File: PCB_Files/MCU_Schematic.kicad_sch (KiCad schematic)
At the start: 34 parts, among them J10 Conn_01x04_Pin, J2 Conn_01x04_Socket, J3 Conn_01x08_Socket, J5 USB_C_Receptacle_USB2.0_16P, J6 Conn_01x04_Socket, J9 Conn_01x04_Socket, SW1 SW_SPDT, U2 STM32F411RETx, Y1 16MHz

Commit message: Swapped all +3.3V and +3.3VA labels to +3V3 and +3V3A lables for clarity.
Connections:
- net +3.3V renamed +3V3
- net +3.3VA renamed +3V3A
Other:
- note added: "+3V31"
- note removed: "+3.31v"

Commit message: Changed pin names on MCU sheet for clarity. Example: US_TIM3_CH1 to US_ECHO
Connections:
- net USB_VSENSE: now reaches R10.1, R9.1, U2.43 (PA10)
- net USB_VBUS: now reaches J5.A4 (VBUS), J5.A9 (VBUS), J5.B4 (VBUS), J5.B9 (VBUS), R9.2
- net TIM2_CH2: now reaches U2.15 (PA1)
- net ECHO_5V: now reaches J2.2 (Pin_2), R3.2
- net US_TIM3_CH1 renamed US_ECHO
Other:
- note removed: "+3V31"
- note removed: "+5V"
- note removed: "+5V Echo"
- note removed: "Use voltage divider for VBUS to GPIO"
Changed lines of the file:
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@@
-		)
-	)
-	(text "Use voltage divider for VBUS to GPIO"
-		(exclude_from_sim no)
-		(at 208.915 67.945 0)
-		(effects
-			(font
-				(size 1.27 1.27)
-			)
 		)
 	)
@@
 		)
 	)
-	(text "+3V31"
-		(exclude_from_sim no)
-		(at 234.315 62.23 0)
-		(effects
-			(font
-				(size 1.016 1.016)
-				(thickness 0.1429)
-			)
-		)
-	)
 	(text "Ultrasonic Sensor"
 		(exclude_from_sim no)
@@
 		)
 	)
-	(text "+5V Echo"
-		(exclude_from_sim no)
-		(at 250.19 36.195 0)
-		(effects
-			(font
-				(size 1.016 1.016)
-				(thickness 0.1429)
-			)
-		)
-	)
-	(text "+5V\n"
+	(text ""
 		(exclude_from_sim no)
 		(at 252.095 67.945 0)
@@
 		)
 	)
-	(text "+3V31"
-		(exclude_from_sim no)
-		(at 230.505 30.48 0)
-		(effects
-			(font
-				(size 1.016 1.016)
-				(thickness 0.1429)
-			)
-		)
-	)
 	(text "OLED Display"
 		(exclude_from_sim no)
@@
 	(wire
 		(pts
+			(xy 133.35 46.99) (xy 147.955 46.99)
+		)
+		(stroke
+			(width 0)
+			(type default)
+		)
+	)
+	(wire
+		(pts
 			(xy 156.845 127) (xy 167.64 127)
 		)
@@
 		)
 	)
-	(label "US_TIM3_CH1"
+	(label "US_ECHO"
 		(at 135.255 59.69 0)
 		(effects
@@
 				(size 1.27 1.27)
 				(thickness 0.254)
+				(bold yes)
+			)
+			(justify left bottom)
+		)
+	)
+	(label "TIM2_CH2"
+		(at 135.255 46.99 0)
+		(effects
+			(font
+				(size 1.27 1.27)
+				(thickness 0.254)
+				(bold yes)
+			)
+			(justify left bottom)
+		)
+	)
+	(label "USB_VBUS"
+		(at 248.92 68.58 0)
+		(effects
+			(font
+				(size 0.762 0.762)
+				(thickness 0.1524)
 				(bold yes)
 			)
@@
 		)
 	)
+	(label "ECHO_5V"
+		(at 245.11 36.83 0)
+		(effects
+			(font
+				(size 1.27 1.27)
+				(thickness 0.254)
+				(bold yes)
+			)
+			(justify left bottom)
+		)
+	)
 	(label "RES"
 		(at 135.255 92.71 0)
@@
 		(effects
 			(font
+				(size 1.27 1.27)
+				(thickness 0.254)
+				(bold yes)
+			)
+			(justify left bottom)
+		)
+	)
+	(label "USB_VSENSE"
+		(at 135.255 69.85 0)
+		(effects
+			(font

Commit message: Began laying out power schematic and motor controller schematic
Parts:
- renumbered U2 to U1
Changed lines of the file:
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@@
 		(in_pos_files yes)
 		(dnp no)
-		(property "Reference" "U2"
+		(property "Reference" "U1"
 			(at 96.52 130.81 0)
 			(show_name no)
@@
 			(project "Sensor_Integration_Board"
 				(path "/0eab3e03-be91-4947-b3db-b5c169582a4b/98354bc1-1342-4ebb-af53-ef072585a9ed"
-					(reference "U2")
+					(reference "U1")
 					(unit 1)
 				)

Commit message: Completed power schematic page. 2S LiPo to buck module to LDO regulator for 3.3v
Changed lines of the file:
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@@
 	)
 	(junction
+		(at 132.715 22.86)
+		(diameter 0)
+		(color 0 0 0 0)
+	)
+	(junction
 		(at 52.07 79.375)
 		(diameter 0)
@@
 	(wire
 		(pts
+			(xy 132.715 22.86) (xy 123.19 22.86)
+		)
+		(stroke
+			(width 0)
+			(type default)
+		)
+	)
+	(wire
+		(pts
 			(xy 97.79 110.49) (xy 87.63 110.49)
 		)
@@
 	(wire
 		(pts
+			(xy 132.715 20.955) (xy 132.715 22.86)
+		)
+		(stroke
+			(width 0)
+			(type default)
+		)
+	)
+	(wire
+		(pts
 			(xy 254.635 41.91) (xy 256.54 41.91)
 		)
@@
 	(wire
 		(pts
-			(xy 139.065 22.86) (xy 123.19 22.86)
+			(xy 139.065 22.86) (xy 132.715 22.86)
 		)
 		(stroke
@@
 					(unit 1)
 				)
+			)
+		)
+	)
+	(symbol
+		(lib_id "power:PWR_FLAG")
+		(at 132.715 20.955 0)
+		(unit 1)
+		(body_style 1)
+		(exclude_from_sim no)
+		(in_bom yes)
+		(on_board yes)
+		(in_pos_files yes)
+		(dnp no)
+		(fields_autoplaced yes)
+		(property "Reference" "#FLG03"
+			(at 132.715 19.05 0)
+			(hide yes)
+			(show_name no)
+			(do_not_autoplace no)
+			(effects
+				(font
+					(size 1.27 1.27)
+				)
+			)
+		)
+		(property "Value" "PWR_FLAG"
+			(at 132.715 16.51 0)
+			(show_name no)
+			(do_not_autoplace no)
+			(effects
+				(font
+					(size 1.27 1.27)
+				)
+			)
+		)
+		(property "Footprint" ""
+			(at 132.715 20.955 0)
+			(hide yes)
+			(show_name no)
+			(do_not_autoplace no)
+			(effects
+				(font
+					(size 1.27 1.27)
+				)
+			)
+		)
+		(property "Datasheet" ""
+			(at 132.715 20.955 0)
+			(hide yes)
+			(show_name no)
+			(do_not_autoplace no)
+			(effects
+				(font
+					(size 1.27 1.27)
+				)
+			)
+		)
+		(property "Description" "Special symbol for telling ERC where power comes from"
+			(at 132.715 20.955 0)
+			(hide yes)
+			(show_name no)
+			(do_not_autoplace no)
+			(effects
+				(font
+					(size 1.27 1.27)
+				)
+			)
+		)
+		(pin "1"
+		)
+		(instances
+			(project "Sensor_Integration_Board"
+				(path "/0eab3e03-be91-4947-b3db-b5c169582a4b/98354bc1-1342-4ebb-af53-ef072585a9ed"
+					(reference "#FLG03")
+					(unit 1)
+				)

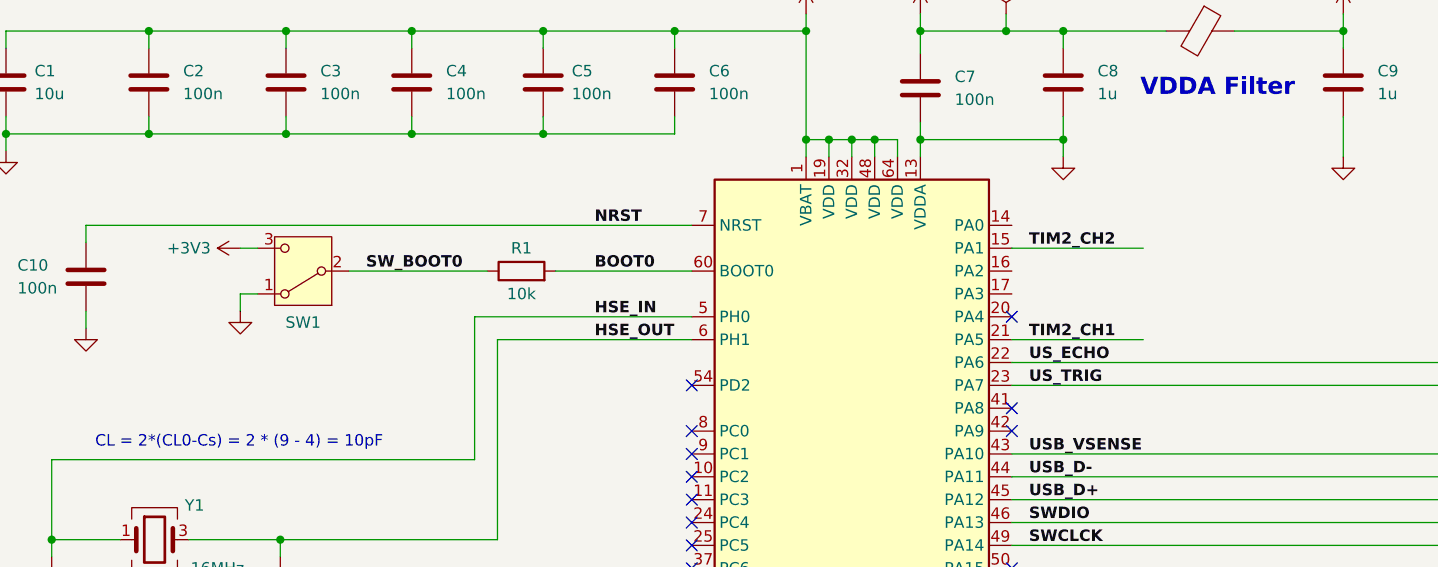
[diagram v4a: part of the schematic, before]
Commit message: Completed motor control schematic sheet and related MCU pin outs.
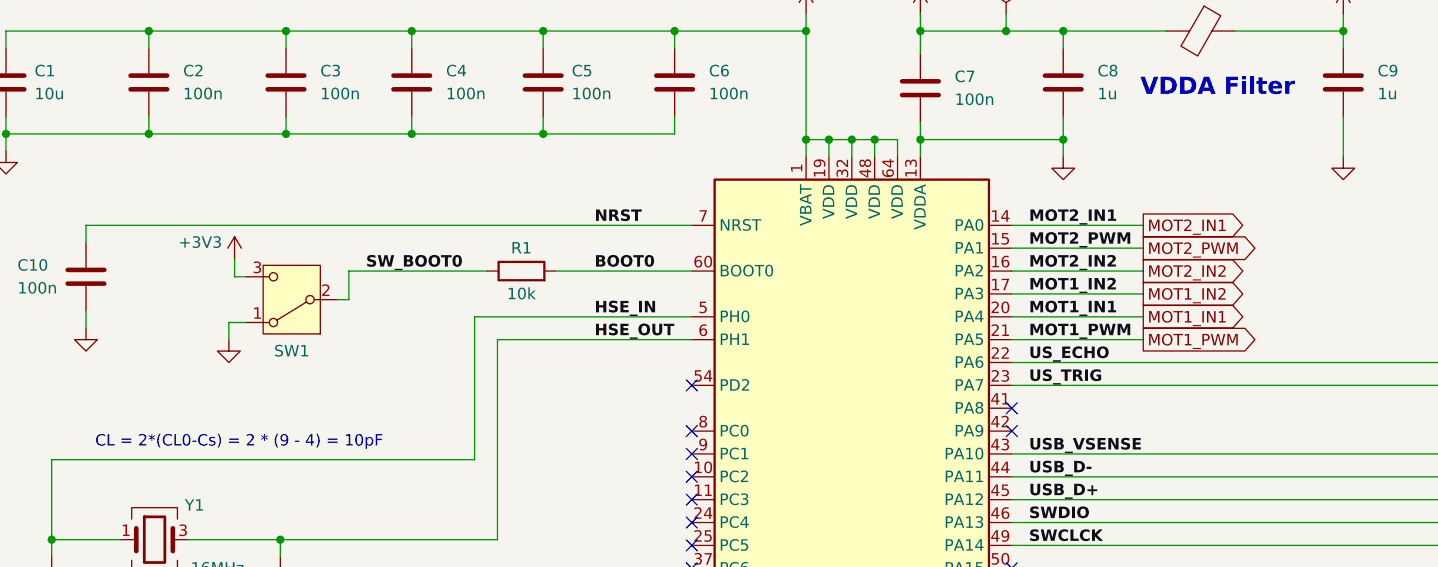
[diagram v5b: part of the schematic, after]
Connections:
- net MOT2_IN1: now reaches U1.14 (PA0)
- net MOT2_IN2: now reaches U1.16 (PA2)
- net MOT1_IN2: now reaches U1.17 (PA3)
- net MOT1_IN1: now reaches U1.20 (PA4)
- net TIM2_CH1 renamed MOT1_PWM
- net TIM2_CH2 renamed MOT2_PWM
- no-connect marks 31 -> 30
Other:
- moved on the sheet: SW1

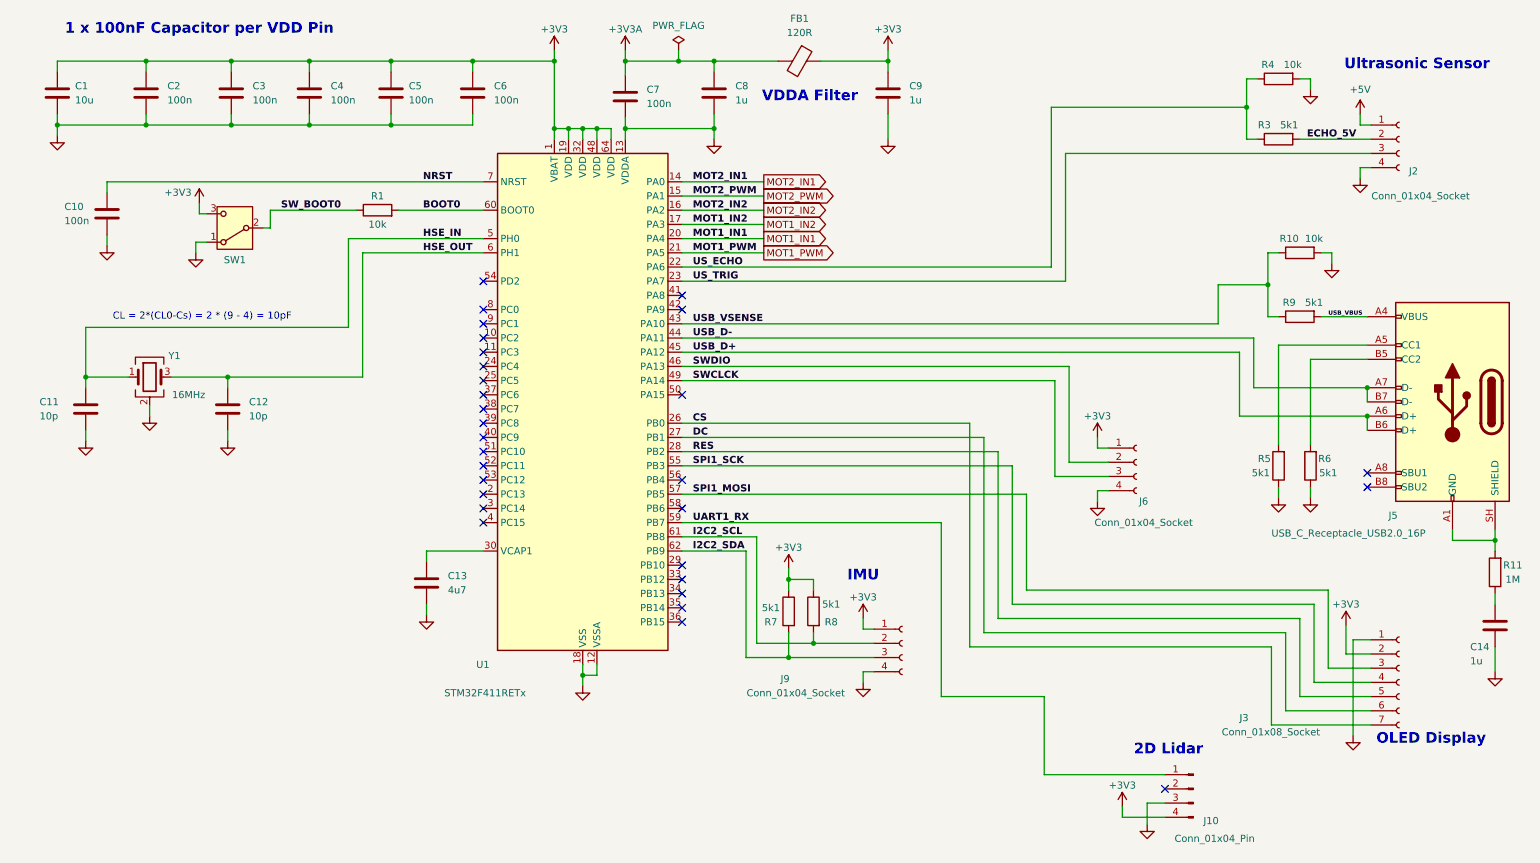
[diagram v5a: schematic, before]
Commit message: Cleaned up all ERC errors and warnings due to missing Power Flags or misaligned grid.
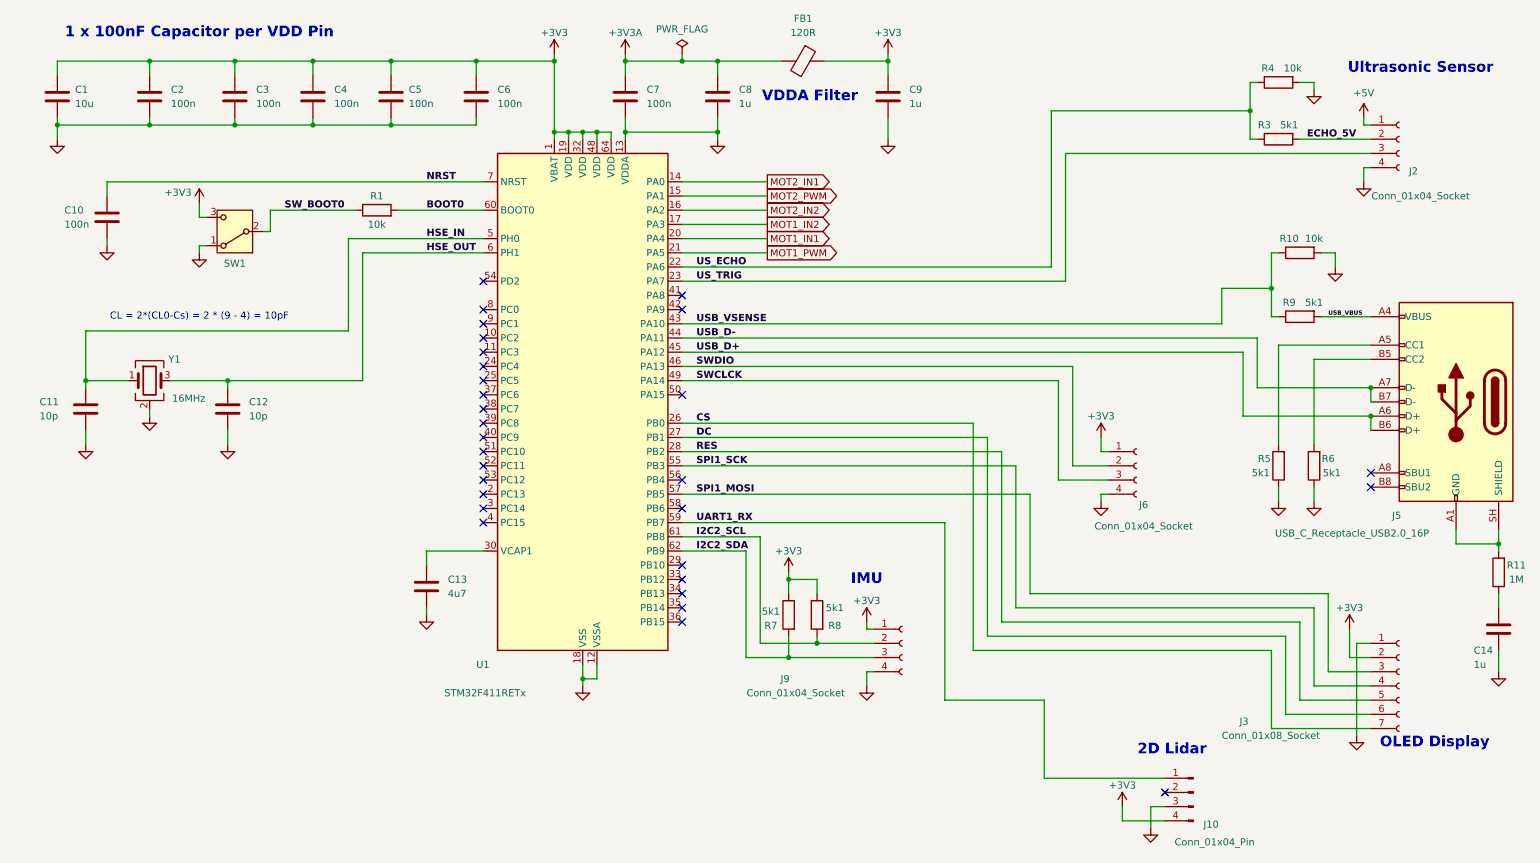
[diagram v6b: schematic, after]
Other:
- moved on the sheet: C1, C10, C13, C14, C2, C3, C4, C5, C6, C8, C9, FB1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

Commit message: General schematic clean up and footprint allocation.
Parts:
- C1, C10, C11, C12, C13, C14, C2, C3, C4, C5, C6, C7, C8: footprint (none) -> Capacitor_SMD:C_0603_1608Metric
- C9: footprint (none) -> Capacitor_SMD:C_0805_2012Metric
- FB1: footprint (none) -> Inductor_SMD:L_0603_1608Metric
- J10: value Conn_01x04_Pin -> 2D_LiDAR
- J2: value Conn_01x04_Socket -> Ultrasonic_Sensor; footprint (none) -> Connector_PinHeader_2.54mm:PinHeader_1x04_P2.54mm_Vertical
- J3: value Conn_01x08_Socket -> OLED_Display; footprint (none) -> Connector_PinSocket_2.54mm:PinSocket_1x07_P2.54mm_Vertical
- J5: footprint (none) -> Custom_Connectors:SAMESKY_UJ20-C-H-G-MSMT-4B-P16-TR
- J6: value Conn_01x04_Socket -> SWD; footprint (none) -> Connector_PinSocket_2.54mm:PinSocket_1x04_P2.54mm_Vertical
- J9: value Conn_01x04_Socket -> IMU; footprint (none) -> Connector_PinSocket_2.54mm:PinSocket_1x04_P2.54mm_Vertical
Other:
- note added: "2D LiDAR"
- note added: "SWD"
- note removed: "2D Lidar"
- moved on the sheet: C1, C10, C11, C12, C13, C14, C2, C3, C4, C5, C6, C7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

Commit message: Added indicator and debug LED's to various outputs such as buck VOUT, ldo regulator VOUT, motor outputs, and status LED for MCU.
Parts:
- added D3: Green, symbol Device:LED
- added R13: 1k, symbol Device:R
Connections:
- net GND: now also R13.2
- net STATUS_LED: now reaches U1.37 (PC6)
- net STATUS_LED: now also D3.2 (A)
- new net: D3.1 (K), R13.1
- no-connect marks 30 -> 29
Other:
- moved on the sheet: C11, C12, J9, R7, R8, Y1
